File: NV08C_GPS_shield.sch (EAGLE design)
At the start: 58 parts, among them IC1 MCP1702-3.3, IC2 74LVC1T45SOT23-HAND, IC3 74LVC1T45SOT23-HAND, IC4 74LVC1T45SOT23-HAND, IC5 74LVC1T45SOT23-HAND, IC6 74LVC1T45SOT23-HAND, IC7 74LVC1T45SOT23-HAND, X1 MEGA2560, X2 CONN-SMATHD-SMD-EDGE, X4 UFL

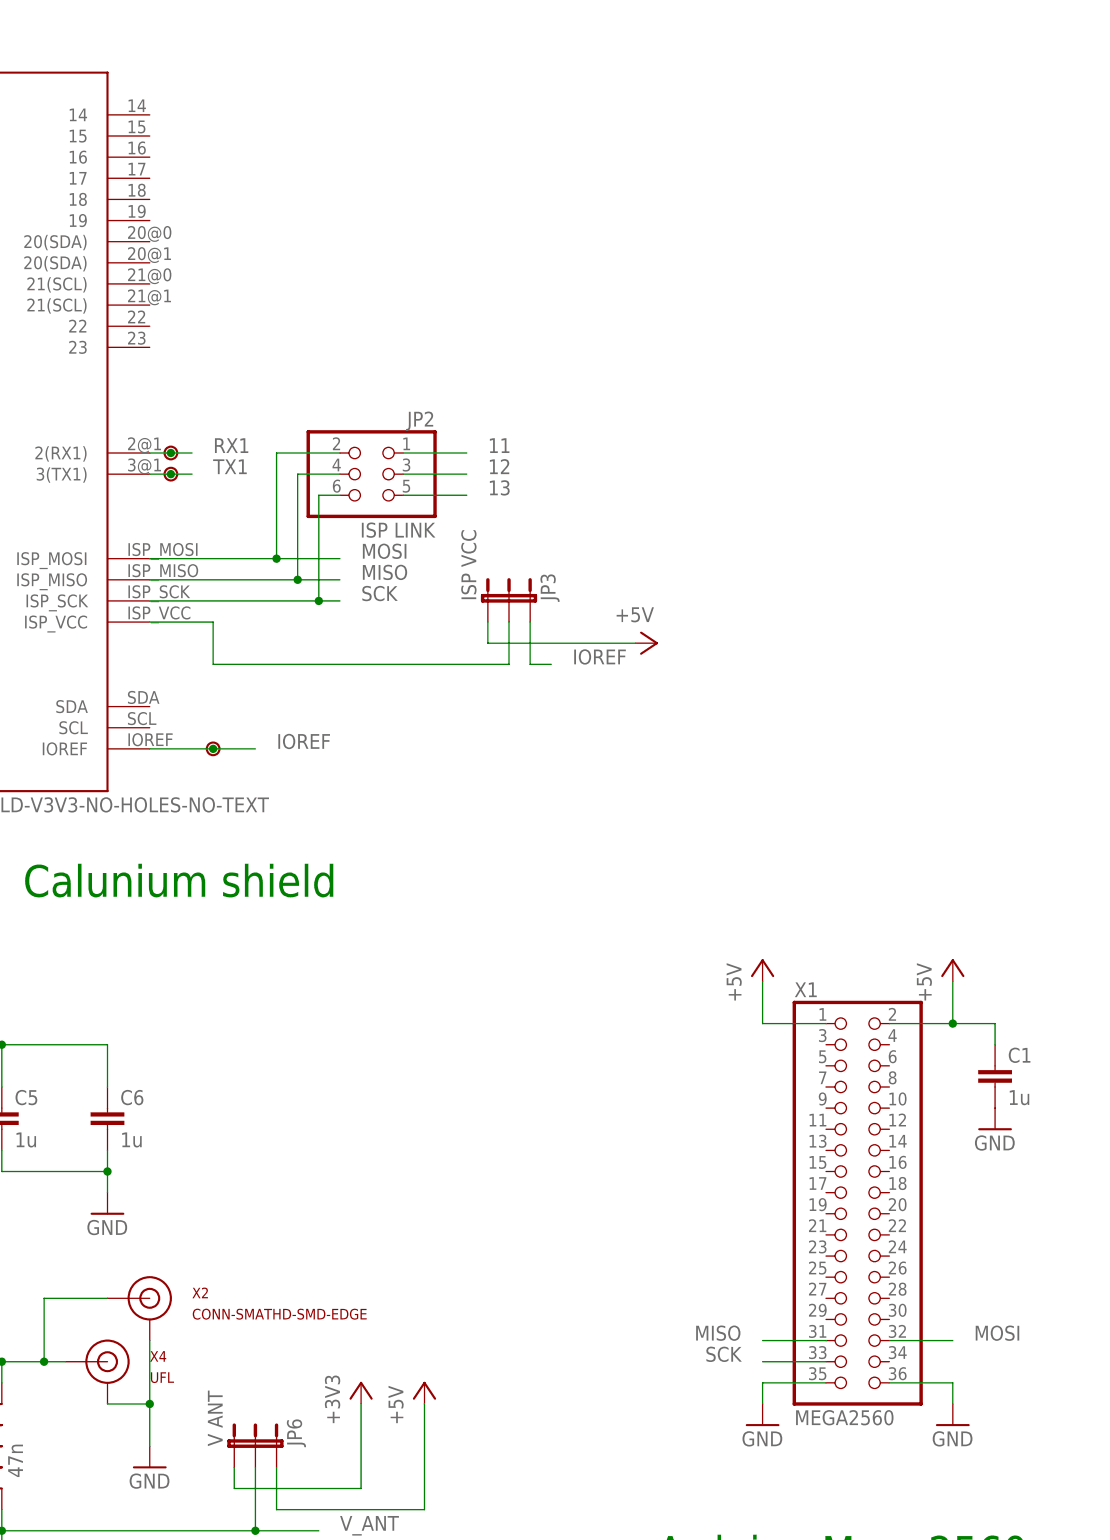
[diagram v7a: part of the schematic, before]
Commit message: Minor routing and silkscreen changes. Extra pads added.
Adding extra pads to access unused Arduino pins for easier hacking.
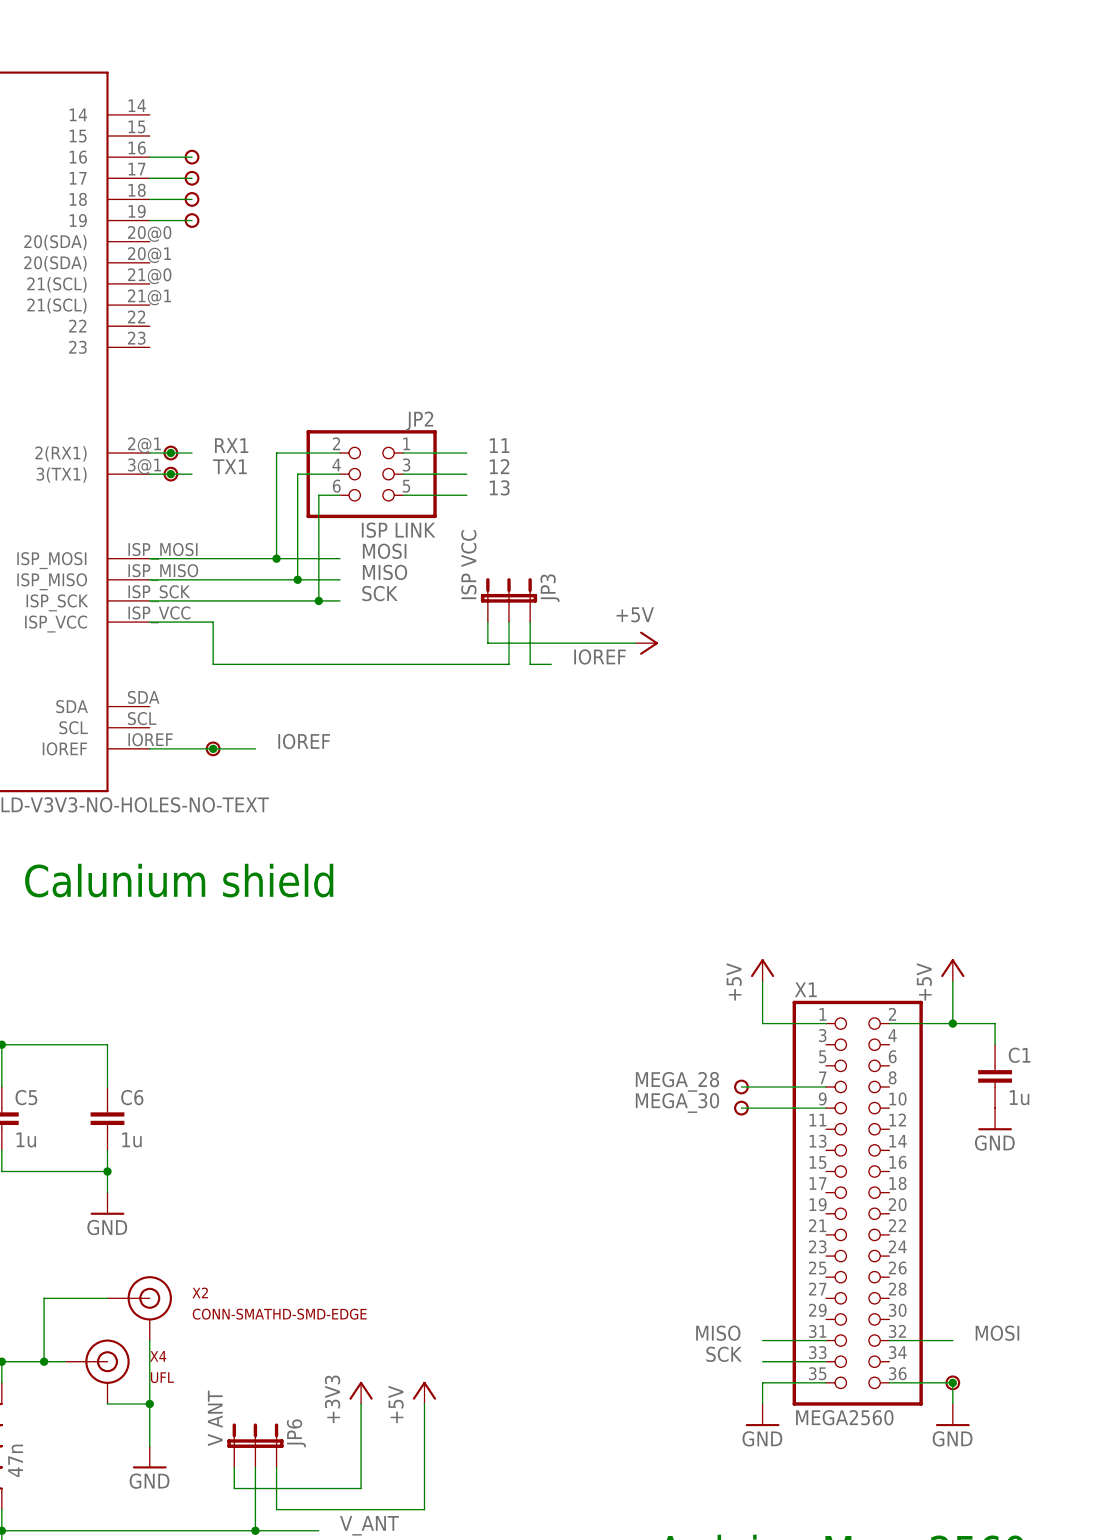
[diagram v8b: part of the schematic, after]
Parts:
- added U$19, U$20, U$21, U$22, U$23, U$24, U$25: PAD, SteveMarple:PAD
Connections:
- net N$20 renamed SLEEP_FLAG
- new net MEGA_28: U$24.1, X1.7
- new net MEGA_30: U$23.1, X1.9
- new net N$10: U$22.1, U$5.16
- new net N$2: U$19.1, U$5.19
- new net N$6: U$20.1, U$5.18
- new net N$9: U$21.1, U$5.17
- net GND: now also U$25.1
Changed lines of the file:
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@@
 <grid distance="0.1" unitdist="inch" unit="inch" style="lines" multiple="1" display="no" altdistance="0.01" altunitdist="inch" altunit="inch"/>
 <layers>
-<layer number="1" name="Top" color="4" fill="1" visible="yes" active="no"/>
-<layer number="2" name="Route2" color="1" fill="3" visible="yes" active="no"/>
-<layer number="3" name="Route3" color="4" fill="3" visible="yes" active="no"/>
-<layer number="14" name="Route14" color="1" fill="6" visible="yes" active="no"/>
-<layer number="15" name="Route15" color="4" fill="6" visible="yes" active="no"/>
-<layer number="16" name="Bottom" color="1" fill="1" visible="yes" active="no"/>
-<layer number="17" name="Pads" color="2" fill="1" visible="yes" active="no"/>
-<layer number="18" name="Vias" color="2" fill="1" visible="yes" active="no"/>
-<layer number="19" name="Unrouted" color="6" fill="1" visible="yes" active="no"/>
-<layer number="20" name="Dimension" color="15" fill="1" visible="yes" active="no"/>
-<layer number="21" name="tPlace" color="7" fill="1" visible="yes" active="no"/>
-<layer number="22" name="bPlace" color="7" fill="1" visible="yes" active="no"/>
-<layer number="23" name="tOrigins" color="15" fill="1" visible="yes" active="no"/>
-<layer number="24" name="bOrigins" color="15" fill="1" visible="yes" active="no"/>
-<layer number="25" name="tNames" color="7" fill="1" visible="yes" active="no"/>
-<layer number="26" name="bNames" color="7" fill="1" visible="yes" active="no"/>
-<layer number="27" name="tValues" color="7" fill="1" visible="yes" active="no"/>
-<layer number="28" name="bValues" color="7" fill="1" visible="yes" active="no"/>
+<layer number="1" name="Top" color="4" fill="1" visible="no" active="no"/>
+<layer number="2" name="Route2" color="1" fill="3" visible="no" active="no"/>
+<layer number="3" name="Route3" color="4" fill="3" visible="no" active="no"/>
+<layer number="14" name="Route14" color="1" fill="6" visible="no" active="no"/>
+<layer number="15" name="Route15" color="4" fill="6" visible="no" active="no"/>
+<layer number="16" name="Bottom" color="1" fill="1" visible="no" active="no"/>
+<layer number="17" name="Pads" color="2" fill="1" visible="no" active="no"/>
+<layer number="18" name="Vias" color="2" fill="1" visible="no" active="no"/>
+<layer number="19" name="Unrouted" color="6" fill="1" visible="no" active="no"/>
+<layer number="20" name="Dimension" color="15" fill="1" visible="no" active="no"/>
+<layer number="21" name="tPlace" color="7" fill="1" visible="no" active="no"/>
+<layer number="22" name="bPlace" color="7" fill="1" visible="no" active="no"/>
+<layer number="23" name="tOrigins" color="15" fill="1" visible="no" active="no"/>
+<layer number="24" name="bOrigins" color="15" fill="1" visible="no" active="no"/>
+<layer number="25" name="tNames" color="7" fill="1" visible="no" active="no"/>
+<layer number="26" name="bNames" color="7" fill="1" visible="no" active="no"/>
+<layer number="27" name="tValues" color="7" fill="1" visible="no" active="no"/>
+<layer number="28" name="bValues" color="7" fill="1" visible="no" active="no"/>
 <layer number="29" name="tStop" color="7" fill="3" visible="no" active="no"/>
 <layer number="30" name="bStop" color="7" fill="6" visible="no" active="no"/>
@@
 <layer number="35" name="tGlue" color="7" fill="4" visible="no" active="no"/>
 <layer number="36" name="bGlue" color="7" fill="5" visible="no" active="no"/>
-<layer number="37" name="tTest" color="7" fill="1" visible="yes" active="no"/>
-<layer number="38" name="bTest" color="7" fill="1" visible="yes" active="no"/>
+<layer number="37" name="tTest" color="7" fill="1" visible="no" active="no"/>
+<layer number="38" name="bTest" color="7" fill="1" visible="no" active="no"/>
 <layer number="39" name="tKeepout" color="4" fill="11" visible="no" active="no"/>
 <layer number="40" name="bKeepout" color="1" fill="11" visible="no" active="no"/>
@@
 <layer number="44" name="Drills" color="7" fill="1" visible="no" active="no"/>
 <layer number="45" name="Holes" color="7" fill="1" visible="no" active="no"/>
-<layer number="46" name="Milling" color="3" fill="1" visible="yes" active="no"/>
-<layer number="47" name="Measures" color="7" fill="1" visible="yes" active="no"/>
-<layer number="48" name="Document" color="7" fill="1" visible="yes" active="no"/>
-<layer number="49" name="Reference" color="7" fill="1" visible="yes" active="no"/>
-<layer number="50" name="dxf" color="7" fill="1" visible="yes" active="no"/>
-<layer number="51" name="tDocu" color="7" fill="1" visible="yes" active="no"/>
-<layer number="52" name="bDocu" color="7" fill="1" visible="yes" active="no"/>
-<layer number="53" name="tGND_GNDA" color="7" fill="9" visible="yes" active="no"/>
-<layer number="54" name="bGND_GNDA" color="1" fill="9" visible="yes" active="no"/>
-<layer number="56" name="wert" color="7" fill="1" visible="yes" active="no"/>
-<layer number="57" name="tCAD" color="7" fill="1" visible="yes" active="no"/>
+<layer number="46" name="Milling" color="3" fill="1" visible="no" active="no"/>
+<layer number="47" name="Measures" color="7" fill="1" visible="no" active="no"/>
+<layer number="48" name="Document" color="7" fill="1" visible="no" active="no"/>
+<layer number="49" name="Reference" color="7" fill="1" visible="no" active="no"/>
+<layer number="50" name="dxf" color="7" fill="1" visible="no" active="no"/>
+<layer number="51" name="tDocu" color="7" fill="1" visible="no" active="no"/>
+<layer number="52" name="bDocu" color="7" fill="1" visible="no" active="no"/>
+<layer number="53" name="tGND_GNDA" color="7" fill="9" visible="no" active="no"/>
+<layer number="54" name="bGND_GNDA" color="1" fill="9" visible="no" active="no"/>
+<layer number="56" name="wert" color="7" fill="1" visible="no" active="no"/>
+<layer number="57" name="tCAD" color="7" fill="1" visible="no" active="no"/>
 <layer number="91" name="Nets" color="2" fill="1" visible="yes" active="yes"/>
 <layer number="92" name="Busses" color="1" fill="1" visible="yes" active="yes"/>
@@
 <part name="U$18" library="SteveMarple" deviceset="PAD" device=""/>
 <part name="X4" library="SteveMarple" deviceset="CONN-UFL" device="HAND" value="UFL"/>
+<part name="U$19" library="SteveMarple" deviceset="PAD" device=""/>
+<part name="U$20" library="SteveMarple" deviceset="PAD" device=""/>
+<part name="U$21" library="SteveMarple" deviceset="PAD" device=""/>
+<part name="U$22" library="SteveMarple" deviceset="PAD" device=""/>
+<part name="U$23" library="SteveMarple" deviceset="PAD" device=""/>
+<part name="U$24" library="SteveMarple" deviceset="PAD" device=""/>
+<part name="U$25" library="SteveMarple" deviceset="PAD" device=""/>
 </parts>
 <sheets>
@@
 <instance part="U$18" gate="G$1" x="208.28" y="157.48"/>
 <instance part="X4" gate="G$1" x="248.92" y="78.74"/>
+<instance part="U$19" gate="G$1" x="259.08" y="215.9"/>
+<instance part="U$20" gate="G$1" x="259.08" y="218.44"/>
+<instance part="U$21" gate="G$1" x="259.08" y="220.98"/>
+<instance part="U$22" gate="G$1" x="259.08" y="223.52"/>
+<instance part="U$23" gate="G$1" x="325.12" y="109.22"/>
+<instance part="U$24" gate="G$1" x="325.12" y="111.76"/>
+<instance part="U$25" gate="G$1" x="350.52" y="76.2"/>
 </instances>
 <busses>
@@
 <wire x1="342.9" y1="76.2" x2="350.52" y2="76.2" width="0.1524" layer="91"/>
 <wire x1="350.52" y1="76.2" x2="350.52" y2="73.66" width="0.1524" layer="91"/>
+<pinref part="U$25" gate="G$1" pin="1"/>
+<junction x="350.52" y="76.2"/>
 </segment>
 <segment>
@@
 </segment>
 </net>
-<net name="N$20" class="0">
+<net name="SLEEP_FLAG" class="0">
 <segment>
 <pinref part="U$7" gate="G$1" pin="1"/>
@@
 </segment>
 </net>
+<net name="N$2" class="0">
+<segment>
+<pinref part="U$5" gate="G$1" pin="19"/>
+<pinref part="U$19" gate="G$1" pin="1"/>
+<wire x1="259.08" y1="215.9" x2="254" y2="215.9" width="0.1524" layer="91"/>
+</segment>
+</net>
+<net name="N$6" class="0">
+<segment>
+<pinref part="U$5" gate="G$1" pin="18"/>
+<pinref part="U$20" gate="G$1" pin="1"/>
+<wire x1="259.08" y1="218.44" x2="254" y2="218.44" width="0.1524" layer="91"/>
+</segment>
+</net>
+<net name="N$9" class="0">
+<segment>
+<pinref part="U$5" gate="G$1" pin="17"/>
+<pinref part="U$21" gate="G$1" pin="1"/>
+<wire x1="259.08" y1="220.98" x2="254" y2="220.98" width="0.1524" layer="91"/>
+</segment>
+</net>
+<net name="N$10" class="0">
+<segment>
+<pinref part="U$5" gate="G$1" pin="16"/>
+<pinref part="U$22" gate="G$1" pin="1"/>
+<wire x1="259.08" y1="223.52" x2="254" y2="223.52" width="0.1524" layer="91"/>
+</segment>
+</net>
+<net name="MEGA_28" class="0">
+<segment>
+<pinref part="X1" gate="A" pin="7"/>
+<pinref part="U$24" gate="G$1" pin="1"/>
+<wire x1="325.12" y1="111.76" x2="335.28" y2="111.76" width="0.1524" layer="91"/>
+<label x="322.58" y="111.76" size="1.778" layer="95" rot="MR0"/>
+</segment>
+</net>
+<net name="MEGA_30" class="0">
+<segment>
+<pinref part="X1" gate="A" pin="9"/>
+<pinref part="U$23" gate="G$1" pin="1"/>
+<wire x1="325.12" y1="109.22" x2="335.28" y2="109.22" width="0.1524" layer="91"/>
+<label x="322.58" y="109.22" size="1.778" layer="95" rot="MR0"/>
+</segment>
+</net>
